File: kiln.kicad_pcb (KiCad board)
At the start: 2 copper layers, 68 parts, among them IC1 PS2702-1-F3-A, J1 SJ2-35813B-SMT-TR, J2 SJ2-35813B-SMT-TR, J3 1935174, J4 1935161, J5 1935161, K1 EE2-12SNUH, Q1 BC817-16, Q2 BC817-16, SW1 SW_Push, U1 LM7805_TO220, U2 TXS0108EPW, U3 LM1117T-3.3, U4 ADS1118IDGS, U5 MAX31856, U6 MAX31856

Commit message: more sch updates
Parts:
- removed A1: Arduino_Nano_v3.x, Module:Arduino_Nano
- removed A2: Arduino_Nano_ESP32, Module:Arduino_Nano
- removed C1, C5: 10uf, Capacitor_SMD:C_0402_1005Metric
- removed C10, C4: 10uf 16v, Capacitor_SMD:C_0402_1005Metric
- removed C11: 0.001uf, Capacitor_SMD:C_0402_1005Metric
- removed C12, C14, C17, C19: 0.01uf, Capacitor_SMD:C_0402_1005Metric
- removed C13, C15, C16, C18, C2, C20, C21, C3, C6, C9: 0.1uf, Capacitor_SMD:C_0402_1005Metric
- removed C7, C8: 10u, Capacitor_SMD:C_0805_2012Metric
- removed D1, D2, D3, D4, D5, D6, D7, D8, D9: SS16FP, SamacSys_Parts:SS12FP
- removed IC1: PS2702-1-F3-A, SamacSys_Parts:SOP254P700X230-4N
- removed J1, J2: SJ2-35813B-SMT-TR, SamacSys_Parts:SJ235813BSMTTR
- removed J3: 1935174, SamacSys_Parts:1935174
- removed J4, J5: 1935161, SamacSys_Parts:1935161
- removed K1: EE2-12SNUH, Relay_SMD:Relay_DPDT_Kemet_EE2_NUH
- removed Q1, Q2: BC817-16, Package_TO_SOT_SMD:SOT-23
- removed R1, R5, R6, R9: 1k, Resistor_SMD:R_0402_1005Metric
- removed R10, R13, R14, R15, R18, R19, R20: 10k, Resistor_SMD:R_0402_1005Metric
- removed R11, R12, R16, R17: 100, Resistor_SMD:R_0402_1005Metric
- removed R2: 220R 1/8W, Resistor_SMD:R_0805_2012Metric
- removed R3, R4: 100R 1W, Resistor_SMD:R_2512_6332Metric
- removed R7, R8: 47k, Resistor_SMD:R_0402_1005Metric
- removed SW1: SW_Push, Button_Switch_SMD:SW_Push_1P1T_NO_E-Switch_TL3301NxxxxxG
- removed U1: LM7805_TO220, Package_TO_SOT_THT:TO-220-3_Vertical
- removed U2: TXS0108EPW, Package_SO:TSSOP-20_4.4x6.5mm_P0.65mm
- removed U3: LM1117T-3.3, Package_TO_SOT_THT:TO-220-3_Vertical
- removed U4: ADS1118IDGS, Package_SO:VSSOP-10_3x3mm_P0.5mm
- removed U5, U6: MAX31856, Package_SO:TSSOP-14_4.4x5mm_P0.65mm

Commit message: progress on pcb
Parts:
- added A1: Arduino_Nano_v3.x, Module:Arduino_Nano, F.Cu at (209.3, 57.8)
- added A2: Arduino_Nano_v3.x, Module:Arduino_Nano, F.Cu at (125.1, 59.0)
- added C1: 10uf 16v, Capacitor_SMD:C_0805_2012Metric, F.Cu at (178.8, 81.3)
- added C10: 0.01uf, Capacitor_SMD:C_0402_1005Metric, F.Cu at (212.5, 47.3)
- added C11: 0.01uf, Capacitor_SMD:C_0402_1005Metric, F.Cu at (121.5, 77.5)
- added C12: 470u 35v, Capacitor_SMD:CP_Elec_10x14.3, F.Cu at (27.8, 69.0)
- added C13: 2.2uF, Capacitor_SMD:C_1206_3216Metric, F.Cu at (37.5, 79.5)
- added C14: 10uf 16v, Capacitor_SMD:C_0805_2012Metric, F.Cu at (85.0, 80.2)
- added C15: 0.1uf, Capacitor_SMD:C_0402_1005Metric, F.Cu at (85.0, 82.7)
- added C16: 0.1uf, Capacitor_SMD:C_0402_1005Metric, F.Cu at (43.5, 87.5)
- added C17: 0.1uf, Capacitor_SMD:C_0402_1005Metric, F.Cu at (77.0, 82.7)
- added C18: 2.2uF, Capacitor_SMD:C_1206_3216Metric, F.Cu at (52.0, 82.5)
- added C19: 10uf 16v, Capacitor_SMD:C_0805_2012Metric, F.Cu at (77.0, 80.2)
- added C2: 0.1uf, Capacitor_SMD:C_0402_1005Metric, F.Cu at (177.8, 83.3)
- added C20: 0.1uf, Capacitor_SMD:C_0402_1005Metric, F.Cu at (51.5, 79.0)
- added C21: 4.7pF, Capacitor_SMD:C_0402_1005Metric, F.Cu at (53.5, 86.0)
- added C22: 0.1uf, Capacitor_SMD:C_0402_1005Metric, F.Cu at (72.0, 82.7)
- added C23: 47uF 16V, Capacitor_SMD:C_1210_3225Metric, F.Cu at (56.5, 87.5)
- added C24: 10uf 16v, Capacitor_SMD:C_0805_2012Metric, F.Cu at (72.0, 80.2)
- added C25: 0.01uf, Capacitor_SMD:C_0402_1005Metric, F.Cu at (170.8, 28.8)
- added C26: 0.1uf, Capacitor_SMD:C_0402_1005Metric, F.Cu at (171.8, 30.8)
- added C27: 0.01uf, Capacitor_SMD:C_0402_1005Metric, F.Cu at (172.8, 28.8)
- added C28: 0.1uf, Capacitor_SMD:C_0402_1005Metric, F.Cu at (167.9, 41.1)
- added C29: 0.1uf, Capacitor_SMD:C_0402_1005Metric, F.Cu at (169.4, 41.1)
- added C3: 0.1uf, Capacitor_SMD:C_0402_1005Metric, F.Cu at (175.4, 83.3)
- added C30: 0.01uf, Capacitor_SMD:C_0402_1005Metric, F.Cu at (98.5, 28.5)
- added C31: 0.1uf, Capacitor_SMD:C_0402_1005Metric, F.Cu at (99.5, 30.5)
- added C32: 0.01uf, Capacitor_SMD:C_0402_1005Metric, F.Cu at (100.5, 28.5)
- added C33: 0.1uf, Capacitor_SMD:C_0402_1005Metric, F.Cu at (95.5, 40.9)
- added C34: 0.1uf, Capacitor_SMD:C_0402_1005Metric, F.Cu at (97.0, 40.9)
- added C35: 0.01uf, Capacitor_SMD:C_0402_1005Metric, F.Cu at (111.0, 28.5)
- added C36: 0.1uf, Capacitor_SMD:C_0402_1005Metric, F.Cu at (112.0, 30.5)
- added C37: 0.01uf, Capacitor_SMD:C_0402_1005Metric, F.Cu at (113.0, 28.5)
- added C38: 0.1uf, Capacitor_SMD:C_0402_1005Metric, F.Cu at (108.0, 40.9)
- added C39: 0.1uf, Capacitor_SMD:C_0402_1005Metric, F.Cu at (109.5, 40.9)
- added C4: 10uf 16v, Capacitor_SMD:C_0805_2012Metric, F.Cu at (174.8, 81.3)
- added C40: 0.01uf, Capacitor_SMD:C_0402_1005Metric, F.Cu at (123.5, 28.5)
- added C41: 0.1uf, Capacitor_SMD:C_0402_1005Metric, F.Cu at (124.5, 30.5)
- added C42: 0.01uf, Capacitor_SMD:C_0402_1005Metric, F.Cu at (125.5, 28.5)
- added C43: 0.1uf, Capacitor_SMD:C_0402_1005Metric, F.Cu at (122.0, 40.9)
- added C44: 0.1uf, Capacitor_SMD:C_0402_1005Metric, F.Cu at (120.5, 40.9)
- added C45: 0.01uf, Capacitor_SMD:C_0402_1005Metric, F.Cu at (136.0, 28.5)
- added C46: 0.1uf, Capacitor_SMD:C_0402_1005Metric, F.Cu at (137.0, 30.5)
- added C47: 0.01uf, Capacitor_SMD:C_0402_1005Metric, F.Cu at (138.0, 28.5)
- added C48: 0.1uf, Capacitor_SMD:C_0402_1005Metric, F.Cu at (134.6, 40.9)
- added C49: 0.1uf, Capacitor_SMD:C_0402_1005Metric, F.Cu at (133.1, 40.9)
- added C5: 0.1uf, Capacitor_SMD:C_0402_1005Metric, F.Cu at (167.3, 83.3)
- added C50: 10uf 16v, Capacitor_SMD:C_0805_2012Metric, F.Cu at (206.5, 42.5)
- added C6: 10uf 16v, Capacitor_SMD:C_0805_2012Metric, F.Cu at (183.8, 34.5)
- added C7: 10uf 16v, Capacitor_SMD:C_0805_2012Metric, F.Cu at (208.0, 34.6)
- added C8: 10uf 16v, Capacitor_SMD:C_0805_2012Metric, F.Cu at (166.8, 81.3)
- added C9: 0.01uf, Capacitor_SMD:C_0402_1005Metric, F.Cu at (212.0, 89.0)
- added D1: SS16FP, SamacSys_Parts:SS12FP, F.Cu at (181.9, 29.0)
- added D10: SS16FP, SamacSys_Parts:SS12FP, F.Cu at (103.0, 45.5)
- added D11: SS16FP, SamacSys_Parts:SS12FP, F.Cu at (116.0, 45.5)
- added D12: SS16FP, SamacSys_Parts:SS12FP, F.Cu at (127.5, 45.5)
- added D13: SS16FP, SamacSys_Parts:SS12FP, F.Cu at (140.0, 45.6)
- added D14: SS16FP, SamacSys_Parts:SS12FP, F.Cu at (96.0, 36.4)
- added D15: SS16FP, SamacSys_Parts:SS12FP, F.Cu at (108.5, 36.5)
- added D16: SS16FP, SamacSys_Parts:SS12FP, F.Cu at (121.0, 36.4)
- added D17: SS16FP, SamacSys_Parts:SS12FP, F.Cu at (133.5, 36.5)
- added D18: SS16FP, SamacSys_Parts:SS12FP, F.Cu at (50.0, 34.6)
- added D19: SMAJ24CA, Diode_SMD:D_SMA, F.Cu at (53.4, 44.7)
- added D2: SS16FP, SamacSys_Parts:SS12FP, F.Cu at (187.4, 29.0)
- added D20: SS16FP, SamacSys_Parts:SS12FP, F.Cu at (29.9, 34.4)
- added D21: SMAJ24CA, Diode_SMD:D_SMA, F.Cu at (33.3, 44.5)
- added D22: SMAJ24CA, Diode_SMD:D_SMA, F.Cu at (27.8, 78.0)
- added D23: SS16FP, SamacSys_Parts:SS12FP, F.Cu at (70.0, 34.6)
- added D24: SMAJ24CA, Diode_SMD:D_SMA, F.Cu at (73.3, 44.7)
- added D25: SS16FP, SamacSys_Parts:SS12FP, F.Cu at (146.3, 34.9)
- added D26: SMAJ24CA, Diode_SMD:D_SMA, F.Cu at (149.7, 45.0)
- added D3: SS16FP, SamacSys_Parts:SS12FP, F.Cu at (206.0, 29.1)
- added D4: SS16FP, SamacSys_Parts:SS12FP, F.Cu at (211.6, 29.1)
- added D5: SS16FP, SamacSys_Parts:SS12FP, F.Cu at (181.4, 32.0)
- added D6: SS16FP, SamacSys_Parts:SS12FP, F.Cu at (187.8, 32.0)
- added D7: SS16FP, SamacSys_Parts:SS12FP, F.Cu at (205.6, 32.1)
- added D8: SS16FP, SamacSys_Parts:SS12FP, F.Cu at (211.9, 32.1)
- added D9: SMAJ24CA, Diode_SMD:D_SMA, F.Cu at (215.5, 47.3)
- added FB1: 74269244182, Inductor_SMD:L_0402_1005Metric_Pad0.77x0.64mm_HandSolder, F.Cu at (168.8, 28.8)
- added FB10: 74269244182, Inductor_SMD:L_0402_1005Metric_Pad0.77x0.64mm_HandSolder, F.Cu at (140.0, 28.5)
- added FB2: 74269244182, Inductor_SMD:L_0402_1005Metric_Pad0.77x0.64mm_HandSolder, F.Cu at (174.8, 28.8)
- added FB3: 74269244182, Inductor_SMD:L_0402_1005Metric_Pad0.77x0.64mm_HandSolder, F.Cu at (96.5, 28.5)
- added FB4: 74269244182, Inductor_SMD:L_0402_1005Metric_Pad0.77x0.64mm_HandSolder, F.Cu at (102.5, 28.5)
- added FB5: 74269244182, Inductor_SMD:L_0402_1005Metric_Pad0.77x0.64mm_HandSolder, F.Cu at (109.0, 28.5)
- added FB6: 74269244182, Inductor_SMD:L_0402_1005Metric_Pad0.77x0.64mm_HandSolder, F.Cu at (115.0, 28.5)
- added FB7: 74269244182, Inductor_SMD:L_0402_1005Metric_Pad0.77x0.64mm_HandSolder, F.Cu at (121.5, 28.5)
- added FB8: 74269244182, Inductor_SMD:L_0402_1005Metric_Pad0.77x0.64mm_HandSolder, F.Cu at (127.5, 28.5)
- added FB9: 74269244182, Inductor_SMD:L_0402_1005Metric_Pad0.77x0.64mm_HandSolder, F.Cu at (134.0, 28.5)
- added IC1: LT8631IFE#PBF, SamacSys_Parts:SOP65P640X120-21N, F.Cu at (45.6, 82.9)
- added J1: 1935161, SamacSys_Parts:1935161, F.Cu at (186.8, 22.5)
- added J10: 1935161, SamacSys_Parts:1935161, F.Cu at (25.3, 86.0)
- added J11: 1935161, SamacSys_Parts:1935161, F.Cu at (174.3, 22.3)
- added J12: 1935161, SamacSys_Parts:1935161, F.Cu at (102.0, 22.0)
- added J13: 1935161, SamacSys_Parts:1935161, F.Cu at (114.5, 22.0)
- added J14: 1935174, SamacSys_Parts:1935174, F.Cu at (84.5, 22.0)
- added J15: 1935161, SamacSys_Parts:1935161, F.Cu at (127.0, 22.0)
- added J16: 1935174, SamacSys_Parts:1935174, F.Cu at (160.8, 22.3)
- added J17: 1935161, SamacSys_Parts:1935161, F.Cu at (139.5, 22.0)
- added J2: 1935161, SamacSys_Parts:1935161, F.Cu at (211.0, 22.6)
- added J3: SJ2-35813B-SMT-TR, SamacSys_Parts:SJ235813BSMTTR, F.Cu at (196.3, 24.5)
- added J4: SJ2-35813B-SMT-TR, SamacSys_Parts:SJ235813BSMTTR, F.Cu at (220.5, 24.6)
- added J5: 1935161, SamacSys_Parts:1935161, F.Cu at (223.0, 49.8)
- added J6: 1935161, SamacSys_Parts:1935161, F.Cu at (148.5, 86.0)
- added J7: 1935161, SamacSys_Parts:1935161, F.Cu at (136.0, 86.0)
- added J8: 1935174, SamacSys_Parts:1935174, F.Cu at (64.5, 22.0)
- added J9: 1935174, SamacSys_Parts:1935174, F.Cu at (44.4, 21.8)
- added K1: EE2-12SNUH, Relay_SMD:Relay_DPDT_Kemet_EE2_NUH, F.Cu at (59.9, 35.1)
- added K2: EE2-12SNUH, Relay_SMD:Relay_DPDT_Kemet_EE2_NUH, F.Cu at (39.7, 34.9)
- added K3: EE2-12SNUH, Relay_SMD:Relay_DPDT_Kemet_EE2_NUH, F.Cu at (79.8, 35.1)
- added K4: EE2-12SNUH, Relay_SMD:Relay_DPDT_Kemet_EE2_NUH, F.Cu at (156.0, 35.4)
- added L1: 15u (14.2u) 2A, Inductor_SMD:L_Chilisin_BMRF00101040, F.Cu at (59.0, 78.0)
- added Q1: BSP296NH6327XTSA1, Package_TO_SOT_SMD:SOT-223-3_TabPin2, F.Cu at (61.0, 44.5)
- added Q2: BSP296NH6327XTSA1, Package_TO_SOT_SMD:SOT-223-3_TabPin2, F.Cu at (40.9, 44.3)
- added Q3: BSP296NH6327XTSA1, Package_TO_SOT_SMD:SOT-223-3_TabPin2, F.Cu at (81.0, 44.5)
- added Q4: BSP296NH6327XTSA1, Package_TO_SOT_SMD:SOT-223-3_TabPin2, F.Cu at (157.3, 44.8)
- added R1: 100R 1W, Resistor_SMD:R_2512_6332Metric, F.Cu at (194.3, 35.5)
- added R10: 10k, Resistor_SMD:R_0402_1005Metric, F.Cu at (173.3, 76.4)
- added R11: 10k, Resistor_SMD:R_0402_1005Metric, F.Cu at (173.3, 54.4)
- added R12: 680, Resistor_SMD:R_0402_1005Metric, F.Cu at (200.5, 77.5)
- added R13: 10k, Resistor_SMD:R_0402_1005Metric, F.Cu at (209.5, 89.0)
- added R14: 1k, Resistor_SMD:R_0402_1005Metric, F.Cu at (191.8, 77.7)
- added R15: 1k, Resistor_SMD:R_0402_1005Metric, F.Cu at (187.0, 77.6)
- added R16: 1k, Resistor_SMD:R_0402_1005Metric, F.Cu at (212.5, 44.8)
- added R17: 680, Resistor_SMD:R_0402_1005Metric, F.Cu at (191.8, 85.2)
- added R18: 680, Resistor_SMD:R_0402_1005Metric, F.Cu at (187.0, 85.1)
- added R19: 10k, Resistor_SMD:R_0402_1005Metric, F.Cu at (125.0, 46.5)
- added R2: 100R 1W, Resistor_SMD:R_2512_6332Metric, F.Cu at (218.5, 35.6)
- added R20: 10k, Resistor_SMD:R_0402_1005Metric, F.Cu at (102.5, 56.0)
- added R21: 10k, Resistor_SMD:R_0402_1005Metric, F.Cu at (118.5, 38.5)
- added R22: 10k, Resistor_SMD:R_0402_1005Metric, F.Cu at (100.0, 56.0)
- added R23: 10k, Resistor_SMD:R_0402_1005Metric, F.Cu at (97.0, 56.0)
- added R24: 10k, Resistor_SMD:R_0402_1005Metric, F.Cu at (95.0, 56.0)
- added R25: 10k, Resistor_SMD:R_0402_1005Metric, F.Cu at (92.5, 56.0)
- added R26: 0, Resistor_SMD:R_0805_2012Metric, F.Cu at (115.5, 49.5)
- added R27: 10k, Resistor_SMD:R_0402_1005Metric, F.Cu at (89.0, 56.0)
- added R28: 10k, Resistor_SMD:R_0402_1005Metric, F.Cu at (88.5, 77.0)
- added R29: 0, Resistor_SMD:R_0805_2012Metric, F.Cu at (115.5, 52.5)
- added R3: 1k, Resistor_SMD:R_0402_1005Metric, F.Cu at (186.8, 34.5)
- added R30: 0, Resistor_SMD:R_0805_2012Metric, F.Cu at (140.5, 69.9)
- added R31: 0, Resistor_SMD:R_0805_2012Metric, F.Cu at (92.0, 78.0)
- added R32: 0, Resistor_SMD:R_0805_2012Metric, F.Cu at (140.5, 74.4)
- added R33: 10k, Resistor_SMD:R_0402_1005Metric, F.Cu at (119.0, 77.5)
- added R34: 1k, Resistor_SMD:R_0402_1005Metric, F.Cu at (110.5, 77.0)
- added R35: 120, Resistor_SMD:R_0402_1005Metric, F.Cu at (145.0, 80.0)
- added R36: 120, Resistor_SMD:R_0402_1005Metric, F.Cu at (66.8, 44.7)
- added R37: 10k, Resistor_SMD:R_0402_1005Metric, F.Cu at (64.3, 49.2)
- added R38: 0, Resistor_SMD:R_1206_3216Metric, B.Cu at (56.5, 28.5)
- added R39: 0, Resistor_SMD:R_1206_3216Metric, B.Cu at (36.4, 28.3)
- added R4: 1k, Resistor_SMD:R_0402_1005Metric, F.Cu at (211.0, 34.6)
- added R40: 120, Resistor_SMD:R_0402_1005Metric, F.Cu at (46.8, 44.5)
- added R41: 10k, Resistor_SMD:R_0402_1005Metric, F.Cu at (44.3, 49.0)
- added R42: 0, Resistor_SMD:R_1206_3216Metric, B.Cu at (76.5, 28.5)
- added R43: 0, Resistor_SMD:R_1206_3216Metric, B.Cu at (152.9, 28.8)
- added R44: 75k, Resistor_SMD:R_0402_1005Metric, F.Cu at (40.5, 79.0)
- added R45: 10k, Resistor_SMD:R_0402_1005Metric, F.Cu at (40.0, 81.0)
- added R46: 8.66k, Resistor_SMD:R_0402_1005Metric, F.Cu at (39.5, 84.5)
- added R47: 422k, Resistor_SMD:R_0402_1005Metric, F.Cu at (52.0, 86.0)
- added R48: 47.5k, Resistor_SMD:R_0402_1005Metric, F.Cu at (52.0, 88.5)
- added R49: 120, Resistor_SMD:R_0402_1005Metric, F.Cu at (169.3, 30.8)
- added R5: 47.5k, Resistor_SMD:R_0402_1005Metric, F.Cu at (183.8, 36.5)
- added R50: 120, Resistor_SMD:R_0402_1005Metric, F.Cu at (174.3, 30.8)
- added R51: 10k, Resistor_SMD:R_0402_1005Metric, F.Cu at (171.4, 42.6)
- added R52: 10k, Resistor_SMD:R_0402_1005Metric, B.Cu at (171.4, 43.6)
- added R53: 10k, Resistor_SMD:R_0402_1005Metric, F.Cu at (171.4, 44.6)
- added R54: 120, Resistor_SMD:R_0402_1005Metric, F.Cu at (97.0, 30.5)
- added R55: 120, Resistor_SMD:R_0402_1005Metric, F.Cu at (102.0, 30.5)
- added R56: 10k, Resistor_SMD:R_0402_1005Metric, F.Cu at (99.0, 42.4)
- added R57: 10k, Resistor_SMD:R_0402_1005Metric, B.Cu at (99.0, 43.4)
- added R58: 10k, Resistor_SMD:R_0402_1005Metric, F.Cu at (99.0, 44.4)
- added R59: 120, Resistor_SMD:R_0402_1005Metric, F.Cu at (109.5, 30.5)
- added R6: 47.5k, Resistor_SMD:R_0402_1005Metric, F.Cu at (208.0, 36.6)
- added R60: 120, Resistor_SMD:R_0402_1005Metric, F.Cu at (114.5, 30.5)
- added R61: 10k, Resistor_SMD:R_0402_1005Metric, F.Cu at (111.5, 42.4)
- added R62: 10k, Resistor_SMD:R_0402_1005Metric, B.Cu at (111.5, 43.4)
- added R63: 10k, Resistor_SMD:R_0402_1005Metric, F.Cu at (111.5, 44.4)
- added R64: 120, Resistor_SMD:R_0402_1005Metric, F.Cu at (86.8, 44.7)
- added R65: 10k, Resistor_SMD:R_0402_1005Metric, F.Cu at (84.3, 49.2)
- added R68: 120, Resistor_SMD:R_0402_1005Metric, F.Cu at (122.0, 30.5)
- added R69: 120, Resistor_SMD:R_0402_1005Metric, F.Cu at (127.0, 30.5)
- added R7: 10k, Resistor_SMD:R_0402_1005Metric, F.Cu at (181.3, 54.4)
- added R70: 10k, Resistor_SMD:R_0402_1005Metric, F.Cu at (124.0, 42.4)
- added R71: 10k, Resistor_SMD:R_0402_1005Metric, B.Cu at (124.0, 43.4)
- added R72: 10k, Resistor_SMD:R_0402_1005Metric, F.Cu at (124.0, 44.4)
- added R73: 120, Resistor_SMD:R_0402_1005Metric, F.Cu at (163.2, 45.0)
- added R74: 10k, Resistor_SMD:R_0402_1005Metric, F.Cu at (160.7, 49.5)
- added R77: 120, Resistor_SMD:R_0402_1005Metric, F.Cu at (134.5, 30.5)
- added R78: 120, Resistor_SMD:R_0402_1005Metric, F.Cu at (139.5, 30.5)
- added R79: 10k, Resistor_SMD:R_0402_1005Metric, F.Cu at (136.6, 42.4)
- added R8: 10k, Resistor_SMD:R_0402_1005Metric, F.Cu at (178.8, 54.4)
- added R80: 10k, Resistor_SMD:R_0402_1005Metric, B.Cu at (136.6, 43.4)
- added R81: 10k, Resistor_SMD:R_0402_1005Metric, F.Cu at (136.6, 44.4)
- added R82: 0, Resistor_SMD:R_1206_3216Metric, F.Cu at (65.0, 28.5)
- added R83: 0, Resistor_SMD:R_1206_3216Metric, F.Cu at (44.9, 28.3)
- added R84: 0, Resistor_SMD:R_1206_3216Metric, F.Cu at (85.0, 28.5)
- added R85: 0, Resistor_SMD:R_1206_3216Metric, F.Cu at (161.3, 28.8)
- added R9: 10k, Resistor_SMD:R_0402_1005Metric, F.Cu at (176.3, 54.4)
- added SW1: SW_Push, Button_Switch_SMD:SW_Push_1P1T_NO_E-Switch_TL3301NxxxxxG, F.Cu at (210.3, 81.8)
- added SW2: SW_Push, Button_Switch_SMD:SW_Push_1P1T_NO_E-Switch_TL3301NxxxxxG, F.Cu at (121.0, 84.5)
- added U1: LM7805_TO220, Package_TO_SOT_THT:TO-220-3_Vertical, F.Cu at (179.4, 86.3)
- added U10: MAX3490xSA, Package_SO:SOIC-8_3.9x4.9mm_P1.27mm, F.Cu at (135.0, 76.5)
- added U11: LM7805_TO220, Package_TO_SOT_THT:TO-220-3_Vertical, F.Cu at (86.1, 86.3)
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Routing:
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- added copper zone on B.Cu, net GND
- added copper zone on F.Cu, net GND
- added copper zone on B.Cu, net GND_Safty
- added copper zone on F.Cu, net GND_Safty
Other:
- board outline added: 211 x 74 mm

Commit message: progress
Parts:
- removed A2: Arduino_Nano_v3.x, Module:Arduino_Nano
- removed FB10, FB9: 74269244182, Inductor_SMD:L_0402_1005Metric_Pad0.77x0.64mm_HandSolder
- removed SW1, SW2: SW_Push, Button_Switch_SMD:SW_Push_1P1T_NO_E-Switch_TL3301NxxxxxG
- removed U13, U14, U15, U16, U17: MAX31856, Package_SO:TSSOP-14_4.4x5mm_P0.65mm
- added C51: 0.1uf, Capacitor_SMD:C_0402_1005Metric, F.Cu at (92.0, 95.8)
- added C52: 10uf 16v, Capacitor_SMD:C_0805_2012Metric, F.Cu at (89.0, 86.0)
- added C53: 470uf 50v, SamacSys_Parts:CAPAE1360X1450N, F.Cu at (88.1, 38.7)
- added C54: 2.2uF, Capacitor_SMD:C_1206_3216Metric, F.Cu at (99.7, 40.6)
- added C55: 0.1uf, Capacitor_SMD:C_0402_1005Metric, F.Cu at (107.1, 31.7)
- added C56: 2.2uF, Capacitor_SMD:C_1206_3216Metric, F.Cu at (99.7, 43.9)
- added C57: 0.1uf, Capacitor_SMD:C_0402_1005Metric, F.Cu at (107.1, 33.7)
- added C58: 4.7pF, Capacitor_SMD:C_0402_1005Metric, F.Cu at (107.1, 35.7)
- added C59: 47uF 16V, Capacitor_SMD:C_1210_3225Metric, F.Cu at (106.3, 57.6)
- added C60: 0.1uf, Capacitor_SMD:C_0402_1005Metric, F.Cu at (107.1, 37.6)
- added C61: 470uf 50v, SamacSys_Parts:CAPAE1360X1450N, F.Cu at (88.1, 7.42)
- added C62: 2.2uF, Capacitor_SMD:C_1206_3216Metric, F.Cu at (99.7, 9.35)
- added C63: 0.1uf, Capacitor_SMD:C_0402_1005Metric, F.Cu at (107.1, 0.48)
- added C64: 2.2uF, Capacitor_SMD:C_1206_3216Metric, F.Cu at (99.7, 12.7)
- added C65: 0.1uf, Capacitor_SMD:C_0402_1005Metric, F.Cu at (107.1, 2.46)
- added C66: 4.7pF, Capacitor_SMD:C_0402_1005Metric, F.Cu at (107.1, 4.42)
- added C67: 47uF 16V, Capacitor_SMD:C_1210_3225Metric, F.Cu at (106.3, 26.3)
- added C68: 0.1uf, Capacitor_SMD:C_0402_1005Metric, F.Cu at (107.1, 6.39)
- added D27: LED, LED_SMD:LED_0402_1005Metric, F.Cu at (106.5, 16.3)
- added IC2: LT8631IFE#PBF, SamacSys_Parts:SOP65P640X120-21N, F.Cu at (101.3, 34.9)
- added IC3: LT8631IFE#PBF, SamacSys_Parts:SOP65P640X120-21N, F.Cu at (101.3, 3.60)
- added J18: 1935161, SamacSys_Parts:1935161, F.Cu at (83.4, 52.1)
- added J19: 1935161, SamacSys_Parts:1935161, F.Cu at (83.4, 20.9)
- added K5: EE2-12NUH, Relay_SMD:Relay_DPDT_Kemet_EE2_NUH, F.Cu at (116.0, 19.9)
- added L2: 4.7uH 3.16A, Inductor_SMD:L_7.3x7.3_H4.5, F.Cu at (100.1, 51.0)
- added L3: 4.7uH 3.16A, Inductor_SMD:L_7.3x7.3_H4.5, F.Cu at (100.1, 19.8)
- added Q5: BSS138P,215, Package_TO_SOT_SMD:SOT-23, F.Cu at (129.0, 13.8)
- added R100: 10k, Resistor_SMD:R_0402_1005Metric, F.Cu at (93.9, 18.3)
- added R101: 8.66k, Resistor_SMD:R_0402_1005Metric, F.Cu at (93.9, 20.3)
- added R102: 475k 1%, Resistor_SMD:R_0402_1005Metric, F.Cu at (93.9, 22.3)
- added R103: 154k 1%, Resistor_SMD:R_0402_1005Metric, F.Cu at (93.9, 24.3)
- added R66: 0, Resistor_SMD:R_1206_3216Metric, B.Cu at (-36.0, 103.5)
- added R67: 0, Resistor_SMD:R_1206_3216Metric, B.Cu at (-42.0, 103.5)
- added R75: 47k, Resistor_SMD:R_0402_1005Metric, F.Cu at (54.7, 123.9)
- added R76: 47k, Resistor_SMD:R_0402_1005Metric, F.Cu at (54.7, 125.9)
- added R86: 47k, Resistor_SMD:R_0402_1005Metric, F.Cu at (84.2, 92.3)
- added R87: 47k, Resistor_SMD:R_0402_1005Metric, F.Cu at (84.2, 94.3)
- added R88: 47k, Resistor_SMD:R_0402_1005Metric, F.Cu at (84.2, 96.3)
- added R89: 1M, Resistor_SMD:R_0402_1005Metric, F.Cu at (84.2, 98.3)
- added R90: 2.2k, Resistor_SMD:R_0805_2012Metric, F.Cu at (104.7, 40.4)
- added R91: 2.2k, Resistor_SMD:R_0805_2012Metric, F.Cu at (104.7, 43.3)
- added R92: 75k, Resistor_SMD:R_0402_1005Metric, F.Cu at (93.9, 47.6)
- added R93: 10k, Resistor_SMD:R_0402_1005Metric, F.Cu at (93.9, 49.6)
- added R94: 8.66k, Resistor_SMD:R_0402_1005Metric, F.Cu at (93.9, 51.6)
- added R95: 475k 1%, Resistor_SMD:R_0402_1005Metric, F.Cu at (93.9, 53.6)
- added R96: 154k 1%, Resistor_SMD:R_0402_1005Metric, F.Cu at (93.9, 55.6)
- added R97: 2.2k, Resistor_SMD:R_0805_2012Metric, F.Cu at (104.7, 9.14)
- added R98: 2.2k, Resistor_SMD:R_0805_2012Metric, F.Cu at (104.7, 12.1)
- added R99: 75k, Resistor_SMD:R_0402_1005Metric, F.Cu at (93.9, 16.3)
- A1: value Arduino_Nano_v3.x -> RaspberryPi_Pico; footprint Module:Arduino_Nano -> Module:RaspberryPi_Pico_Common_Unspecified
- C1, C24, C4, C6: value 10uf 16v -> 0.1uf; footprint Capacitor_SMD:C_0805_2012Metric -> Capacitor_SMD:C_0402_1005Metric
- C10: value 0.01uf -> 2.2uF; footprint Capacitor_SMD:C_0402_1005Metric -> Capacitor_SMD:C_1206_3216Metric
- C11, C27, C30, C37, C40, C45: value 0.01uf -> 0.1uf
- C12: value 470u 35v -> 2.2uF; footprint Capacitor_SMD:CP_Elec_10x14.3 -> Capacitor_SMD:C_1206_3216Metric
- C13, C18: value 2.2uF -> 0.1uf; footprint Capacitor_SMD:C_1206_3216Metric -> Capacitor_SMD:C_0402_1005Metric
- C14, C50, C7, C8: value 10uf 16v -> 4.7pF; footprint Capacitor_SMD:C_0805_2012Metric -> Capacitor_SMD:C_0402_1005Metric
- C15: value 0.1uf -> 47uF 16V; footprint Capacitor_SMD:C_0402_1005Metric -> Capacitor_SMD:C_1210_3225Metric
- C17, C20, C26, C29, C3, C31, C36, C38, C39: value 0.1uf -> 0.01uf
- C19: value 10uf 16v -> 0.01uf; footprint Capacitor_SMD:C_0805_2012Metric -> Capacitor_SMD:C_0402_1005Metric
- C2: value 0.1uf -> 2.2uF; footprint Capacitor_SMD:C_0402_1005Metric -> Capacitor_SMD:C_1206_3216Metric
- C21: value 4.7pF -> 0.1uf
- C23: value 47uF 16V -> 0.01uf; footprint Capacitor_SMD:C_1210_3225Metric -> Capacitor_SMD:C_0402_1005Metric
- C35, C42, C47: value 0.01uf -> 4.7pF
- C43, C44: value 0.1uf -> 4.7pF
- C46, C49: value 0.1uf -> 10uf 16v; footprint Capacitor_SMD:C_0402_1005Metric -> Capacitor_SMD:C_0805_2012Metric
- C9: value 0.01uf -> 470uf 50v; footprint Capacitor_SMD:C_0402_1005Metric -> SamacSys_Parts:CAPAE1360X1450N
- D11, D2, D4, D7: value SS16FP -> SMAJ24CA; footprint SamacSys_Parts:SS12FP -> Diode_SMD:D_SMA
- D12, D13, D16, D17, D20: value SS16FP -> BZX84C3V3LT1G; footprint SamacSys_Parts:SS12FP -> Package_TO_SOT_SMD:SOT-23
- D19, D22: value SMAJ24CA -> SS16FP; footprint Diode_SMD:D_SMA -> SamacSys_Parts:SS12FP
- D21: value SMAJ24CA -> BZX84C3V3LT1G; footprint Diode_SMD:D_SMA -> Package_TO_SOT_SMD:SOT-23
- D25, D5: value SS16FP -> LED; footprint SamacSys_Parts:SS12FP -> LED_SMD:LED_0402_1005Metric
- J10, J11: value 1935161 -> 1935174; footprint SamacSys_Parts:1935161 -> SamacSys_Parts:1935174
- J13, J15, J17: value 1935161 -> SJ2-35813B-SMT-TR; footprint SamacSys_Parts:1935161 -> SamacSys_Parts:SJ235813BSMTTR
- J14, J16, J9: value 1935174 -> 1935161; footprint SamacSys_Parts:1935174 -> SamacSys_Parts:1935161
- J2: value 1935161 -> Conn_01x10_Pin; footprint SamacSys_Parts:1935161 -> Connector_JST:JST_XH_B10B-XH-AM_1x10_P2.50mm_Vertical
- J3, J4: value SJ2-35813B-SMT-TR -> 1935174; footprint SamacSys_Parts:SJ235813BSMTTR -> SamacSys_Parts:1935174
- K1, K2, K3, K4: value EE2-12SNUH -> EE2-12NUH
- L1: value 15u (14.2u) 2A -> 22uH Shld 20% 1.9A MSD1048-223MED; footprint Inductor_SMD:L_Chilisin_BMRF00101040 -> Inductor_SMD:L_Bourns_SRP1038C_10.0x10.0mm
- Q1, Q2, Q3, Q4: value BSP296NH6327XTSA1 -> BSS138P,215; footprint Package_TO_SOT_SMD:SOT-223-3_TabPin2 -> Package_TO_SOT_SMD:SOT-23
- R1, R2: value 100R 1W -> 10k; footprint Resistor_SMD:R_2512_6332Metric -> Resistor_SMD:R_0402_1005Metric
- R10, R8, R9: value 10k -> 1k
- R11, R7: value 10k -> 390
- R12: value 680 -> 390
- R14, R3, R34, R4: value 1k -> 10k
- R16: value 1k -> 2.2k
- R17: value 680 -> 2.2k
- R18: value 680 -> 10k
- R26, R29, R30, R31, R32: value 0 -> 10k; footprint Resistor_SMD:R_0805_2012Metric -> Resistor_SMD:R_0402_1005Metric
- R33, R37: value 10k -> 120
- R35, R36, R40, R59, R60: value 120 -> 0; footprint Resistor_SMD:R_0402_1005Metric -> Resistor_SMD:R_1206_3216Metric
- R38: value 0 -> 10k; footprint Resistor_SMD:R_1206_3216Metric -> Resistor_SMD:R_0402_1005Metric; moved to F.Cu
- R39: moved to F.Cu
- R41: value 10k -> 2.2k; footprint Resistor_SMD:R_0402_1005Metric -> Resistor_SMD:R_0805_2012Metric
- R42: value 0 -> 2.2k; footprint Resistor_SMD:R_1206_3216Metric -> Resistor_SMD:R_0805_2012Metric; moved to F.Cu
- R43: value 0 -> 75k; footprint Resistor_SMD:R_1206_3216Metric -> Resistor_SMD:R_0402_1005Metric; moved to F.Cu
- R44: value 75k -> 10k
- R45: value 10k -> 8.66k
- R46: value 8.66k -> 475k 1%
- R47: value 422k -> 90.7k 1%
- R48: value 47.5k -> 2k
- R49, R50, R54, R55: value 120 -> 2k
- R5, R6: value 47.5k -> 10k
- R51, R53, R56, R61, R63: value 10k -> 2k
- R52, R62: value 10k -> 2k; moved to F.Cu
- R57: value 10k -> 120; moved to F.Cu
- R69: value 120 -> 10k
- R70: value 10k -> 0; footprint Resistor_SMD:R_0402_1005Metric -> Resistor_SMD:R_1206_3216Metric
- R71: value 10k -> 0; footprint Resistor_SMD:R_0402_1005Metric -> Resistor_SMD:R_1206_3216Metric; moved to F.Cu
- R72: value 10k -> 100R 1W; footprint Resistor_SMD:R_0402_1005Metric -> Resistor_SMD:R_2512_6332Metric
- R73: value 120 -> 475k
- R74, R81: value 10k -> 47k
- R77: value 120 -> 1M
- R78: value 120 -> 100R 1W; footprint Resistor_SMD:R_0402_1005Metric -> Resistor_SMD:R_2512_6332Metric
- R79: value 10k -> 475k
- R80: value 10k -> 47k; moved to F.Cu
- R82: value 0 -> 47k; footprint Resistor_SMD:R_1206_3216Metric -> Resistor_SMD:R_0402_1005Metric
- R83: value 0 -> 1M; footprint Resistor_SMD:R_1206_3216Metric -> Resistor_SMD:R_0402_1005Metric
- R84: value 0 -> 100R 1W; footprint Resistor_SMD:R_1206_3216Metric -> Resistor_SMD:R_2512_6332Metric
- R85: value 0 -> 475k; footprint Resistor_SMD:R_1206_3216Metric -> Resistor_SMD:R_0402_1005Metric
- U1: value LM7805_TO220 -> TCMT1109; footprint Package_TO_SOT_THT:TO-220-3_Vertical -> Package_SO:SOP-4_4.4x2.6mm_P1.27mm
- U10: value MAX3490xSA -> LMV321; footprint Package_SO:SOIC-8_3.9x4.9mm_P1.27mm -> Package_TO_SOT_SMD:SOT-353_SC-70-5
- U11: value LM7805_TO220 -> LMV321; footprint Package_TO_SOT_THT:TO-220-3_Vertical -> Package_TO_SOT_SMD:SOT-353_SC-70-5
- U12: value LM1117T-3.3 -> LMV321; footprint Package_TO_SOT_THT:TO-220-3_Vertical -> Package_TO_SOT_SMD:SOT-353_SC-70-5
- U2: value LM1117T-3.3 -> TCMT1109; footprint Package_TO_SOT_THT:TO-220-3_Vertical -> Package_SO:SOP-4_4.4x2.6mm_P1.27mm
- U3: value ADS1118IDGS -> TCMT1109; footprint Package_SO:VSSOP-10_3x3mm_P0.5mm -> Package_SO:SOP-4_4.4x2.6mm_P1.27mm
- U4: value TCMT1109 -> ESP32-S3-DevKitC; footprint Package_SO:SOP-4_4.4x2.6mm_P1.27mm -> PCM_Espressif:ESP32-S3-DevKitC
- U5: value TCMT1109 -> SX1509; footprint Package_SO:SOP-4_4.4x2.6mm_P1.27mm -> PCM_SparkFun-Semiconductor-Standard:QFN-28-1EP_4x4mm_P0.4mm_EP2.6x2.6mm
- U6: value TCMT1109 -> MAX31856; footprint Package_SO:SOP-4_4.4x2.6mm_P1.27mm -> Package_SO:TSSOP-14_4.4x5mm_P0.65mm
- U7, U8, U9: value TXS0108EPW -> MAX31856; footprint Package_SO:TSSOP-20_4.4x6.5mm_P0.65mm -> Package_SO:TSSOP-14_4.4x5mm_P0.65mm
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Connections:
- A1 pad 1: unconnected-(A1-D1/TX-Pad1) -> /SaftyProcessor/MISO
- A1 pad 12: /SaftyProcessor/CS1 -> /SaftyProcessor/estop
- A1 pad 13: /SaftyProcessor/CS0 -> GND_Safty
- A1 pad 14: /SaftyProcessor/MOSI -> /SaftyProcessor/fault
- A1 pad 15: /SaftyProcessor/MISO -> unconnected-(A1-GPIO11-Pad15)
- A1 pad 16: /SaftyProcessor/CLK -> unconnected-(A1-GPIO12-Pad16)
- A1 pad 18: unconnected-(A1-AREF-Pad18) -> GND_Safty
- A1 pad 2: unconnected-(A1-D0/RX-Pad2) -> /SaftyProcessor/CS0
- A1 pad 21: Net-(A1-A2) -> unconnected-(A1-GPIO16-Pad21)
- A1 pad 22: Net-(A1-A3) -> unconnected-(A1-GPIO17-Pad22)
- A1 pad 23: Net-(A1-A4) -> GND_Safty
- A1 pad 24: Net-(A1-A5) -> unconnected-(A1-GPIO18-Pad24)
- A1 pad 27: 5v_Safty -> unconnected-(A1-GPIO21-Pad27)
- A1 pad 28: Net-(A1-~{RESET}-Pad28) -> GND_Safty
- A1 pad 29: GND_Safty -> unconnected-(A1-GPIO22-Pad29)
- A1 pad 3: unconnected-(A1-~{RESET}-Pad3) -> GND_Safty
- A1 pad 4: GND_Safty -> /SaftyProcessor/CLK
- A1 pad 5: unconnected-(A1-D2-Pad5) -> /SaftyProcessor/MOSI
- A1 pad 6: unconnected-(A1-D3-Pad6) -> /SaftyProcessor/PicoTx
- A1 pad 7: unconnected-(A1-D4-Pad7) -> /SaftyProcessor/PicoRx
- A1 pad 8: unconnected-(A1-D5-Pad8) -> GND_Safty
- C1 pad 1: 8V -> 3.3v_Safty
- C10 pad 1: Net-(A1-A2) -> 12V_Main
- C10 pad 2: GND_Safty -> GND_Main
- C11 pad 1: Net-(A2-~{RESET}-Pad28) -> Net-(IC1-TR/SS)
- C11 pad 2: GND -> GND_Main
- C12 pad 1: 12V -> Net-(IC1-INTVCC)
- C12 pad 2: GND -> GND_Main
- C13 pad 1: 12V -> Net-(IC1-SW)
- C13 pad 2: GND -> Net-(IC1-BST)
- C14 pad 1: 8V -> 5V_Main
- C14 pad 2: GND -> Net-(IC1-FB)
- C15 pad 1: 8V -> GND_Main
- C15 pad 2: GND -> 5V_Main
- C16 pad 1: Net-(IC1-TR/SS) -> 5V_Main
- C16 pad 2: GND -> GND_Main
- C17 pad 1: 5V -> GND_Safty
- C17 pad 2: GND -> Net-(U6-T+)
- C18 pad 1: Net-(IC1-INTVCC) -> Net-(U6-T+)
- C18 pad 2: GND -> Net-(U6-T-)
- C19 pad 1: 5V -> Net-(U6-T-)
- C19 pad 2: GND -> GND_Safty
- C2 pad 1: 8V -> Net-(A1-ADC_VREF)
- C20 pad 1: Net-(IC1-SW) -> Net-(U6-BIAS)
- C20 pad 2: Net-(IC1-BST) -> GND_Safty
- C21 pad 1: 8V -> 3.3v_Safty
- C21 pad 2: Net-(IC1-FB) -> GND_Safty
- C22 pad 1: 3.3V -> 3.3v_Safty
- C22 pad 2: GND -> GND_Safty
- C23 pad 1: GND -> GND_Main
- C23 pad 2: 8V -> Net-(U7-T+)
- C24 pad 1: 3.3V -> Net-(U7-T+)
- C24 pad 2: GND -> Net-(U7-T-)
- C25 pad 1: GND_Safty -> Net-(U7-T-)
- C25 pad 2: Net-(U13-T+) -> GND_Main
- C26 pad 1: Net-(U13-T+) -> Net-(U7-BIAS)
- C26 pad 2: Net-(U13-T-) -> GND_Main
- C27 pad 1: Net-(U13-T-) -> 3.3V_Main
- C27 pad 2: GND_Safty -> GND_Main
- C28 pad 1: 3.3v_Safty -> 3.3V_Main
- C28 pad 2: GND_Safty -> GND_Main
- C29 pad 1: 3.3v_Safty -> GND_Main
- C29 pad 2: GND_Safty -> Net-(U8-T+)
- C3 pad 1: 5v_Safty -> /SaftyProcessor/estop
- C30 pad 1: GND -> Net-(U8-T+)
- C30 pad 2: Net-(U14-T+) -> Net-(U8-T-)
- C31 pad 1: Net-(U14-T+) -> Net-(U8-T-)
- C31 pad 2: Net-(U14-T-) -> GND_Main
- C32 pad 1: Net-(U14-T-) -> Net-(U8-BIAS)
- C32 pad 2: GND -> GND_Main
- C33 pad 1: 3.3V -> 3.3V_Main
- C33 pad 2: GND -> GND_Main
- C34 pad 1: 3.3V -> 3.3V_Main
- C34 pad 2: GND -> GND_Main
- C35 pad 1: GND -> Net-(D7-A2)
- C35 pad 2: Net-(U15-T+) -> GND_Main
- C36 pad 1: Net-(U15-T+) -> GND_Main
- C36 pad 2: Net-(U15-T-) -> Net-(U9-T+)
- C37 pad 1: Net-(U15-T-) -> Net-(U9-T+)
- C37 pad 2: GND -> Net-(U9-T-)
- C38 pad 1: 3.3V -> Net-(U9-T-)
- C38 pad 2: GND -> GND_Main
- C39 pad 1: 3.3V -> Net-(U9-BIAS)
- C39 pad 2: GND -> GND_Main
- C4 pad 1: 5v_Safty -> 3.3V_Main
- C4 pad 2: GND_Safty -> GND_Main
- C40 pad 1: GND -> 3.3V_Main
- C40 pad 2: Net-(U16-T+) -> GND_Main
- C41 pad 1: Net-(U16-T+) -> 3.3V_Main
- C41 pad 2: Net-(U16-T-) -> GND_Main
- C42 pad 1: Net-(U16-T-) -> Net-(D9-A2)
- C42 pad 2: GND -> GND_Safty
- C43 pad 1: 3.3V -> Net-(D11-A2)
- C43 pad 2: GND -> GND_Main
- C44 pad 1: 3.3V -> Net-(D12-K)
- C44 pad 2: GND -> Net-(D13-K)
- C45 pad 1: GND -> 3.3v_Safty
- C45 pad 2: Net-(U17-T+) -> GND_Safty
- C46 pad 1: Net-(U17-T+) -> /SaftyProcessor/Current1
- C46 pad 2: Net-(U17-T-) -> GND_Safty
- C47 pad 1: Net-(U17-T-) -> Net-(D16-K)
- C47 pad 2: GND -> Net-(D17-K)
- C48 pad 1: 3.3V -> 3.3v_Safty
- C48 pad 2: GND -> GND_Safty
- C49 pad 1: 3.3V -> /SaftyProcessor/Current2
- C49 pad 2: GND -> GND_Safty
- C5 pad 1: 3.3v_Safty -> 3.3V_Main
- C5 pad 2: GND_Safty -> GND_Main
- C50 pad 1: 5v_Safty -> Net-(D20-K)
- C50 pad 2: GND_Safty -> Net-(D21-K)
- C6 pad 1: Net-(U3-AIN0) -> 5V_Main
- C6 pad 2: GND_Safty -> GND_Main
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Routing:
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- removed copper zone on B.Cu, net GND
- removed copper zone on F.Cu, net GND
- removed copper zone on B.Cu, net GND_Safty
- removed copper zone on F.Cu, net GND_Safty
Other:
- board outline removed

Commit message: progress
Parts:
- C26, C27, C28, R35, R36, R39, R40, R53, R59, R60, R70, R71: moved to B.Cu
- moved C43 212.8 mm to (-81.0, 57.0)
- moved Q5 211.7 mm to (-78.0, 58.0), turned to 180 degrees
- moved R71 208.5 mm to (-83.0, 43.5), turned to 90 degrees
- moved D11 207.2 mm to (-79.5, 54.0), turned to 180 degrees
- moved R68 206.6 mm to (-74.5, 59.0)
- moved R69 206.4 mm to (-75.0, 57.0), turned to -90 degrees
- moved D10 205.6 mm to (-79.5, 50.5), turned to 180 degrees
- moved R70 203.0 mm to (-77.0, 43.5), turned to 90 degrees
- moved C17 200.8 mm to (-65.5, 104.9)
- moved C18 200.8 mm to (-65.5, 106.9)
- moved C19 200.8 mm to (-65.5, 108.9)
- moved C20 200.8 mm to (-65.5, 110.8)
- moved C21 200.8 mm to (-65.5, 112.8)
- moved C22 200.8 mm to (-65.5, 114.8)
- moved FB1 200.8 mm to (-66.8, 117.0)
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
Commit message: small changes
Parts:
- added J20: 1935161, SamacSys_Parts:1935161, F.Cu at (-63.5, -54.3)
- added J21: 1935161, SamacSys_Parts:1935161, F.Cu at (-63.5, -42.2)
- added J23: 1935161, SamacSys_Parts:1935161, F.Cu at (-63.5, -30.1)
- added J24: 1935161, SamacSys_Parts:1935161, F.Cu at (-63.5, -18.0)
- added J25: 1935161, SamacSys_Parts:1935161, F.Cu at (-63.5, -5.86)
- moved R19 56.3 mm to (55.3, -40.4)
- moved R28 56.3 mm to (61.1, -42.4)
- moved R21 56.3 mm to (55.3, -36.4)
- moved R24 56.3 mm to (58.2, -40.4)
- moved R26 56.3 mm to (58.2, -36.4)
- moved R30 56.3 mm to (61.1, -38.4)
- moved R31 56.3 mm to (61.1, -36.4)
- moved R20 31.3 mm to (29.6, -19.0)
- moved R23 31.3 mm to (32.5, -23.0)
- moved R25 31.3 mm to (32.5, -19.0)
- moved R29 31.3 mm to (35.4, -21.0)
- moved R27 31.3 mm to (32.5, -15.0)
- moved R32 31.3 mm to (35.4, -15.0)
- moved C36 30.5 mm to (-73.7, 88.0)
- moved FB7 19.5 mm to (-73.2, 85.0)
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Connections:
- U5 pad 16: unconnected-(U5-I/O[11]-Pad16) -> /MainControler/IO_5
- U5 pad 19: unconnected-(U5-I/O[12]-Pad19) -> /MainControler/IO_6
- U5 pad 20: unconnected-(U5-I/O[13]-Pad20) -> /MainControler/IO_7
- U5 pad 5: unconnected-(U5-I/O[4]-Pad5) -> /MainControler/IO_1
- U5 pad 6: unconnected-(U5-I/O[5]-Pad6) -> /MainControler/IO_2
- U5 pad 7: unconnected-(U5-I/O[6]-Pad7) -> /MainControler/IO_3
- U5 pad 8: unconnected-(U5-I/O[7]-Pad8) -> /MainControler/IO_4

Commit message: progress
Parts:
- moved FB1 123.5 mm to (-184.3, 79.3)
- moved C17 121.4 mm to (-184.8, 82.3)
- moved FB2 121.3 mm to (-181.3, 79.3), turned to 180 degrees
- moved C20 121.0 mm to (-183.3, 83.3), turned to 180 degrees
- moved C22 120.6 mm to (-182.8, 86.8)
- moved C21 120.4 mm to (-182.8, 85.8)
- moved R48 120.1 mm to (-184.3, 80.8)
- moved C18 119.9 mm to (-182.9, 82.3)
- moved R50 119.8 mm to (-182.8, 81.3), turned to 90 degrees
- moved C19 118.3 mm to (-180.8, 82.3)
- moved R49 117.9 mm to (-181.3, 80.8), turned to 180 degrees
- moved U6 112.2 mm to (-183.3, 87.8), turned to -90 degrees
- moved J5 110.3 mm to (-180.3, 73.8)
- moved C43 100.2 mm to (-176.9, 28.1)
- moved D10 100.2 mm to (-175.4, 21.6)
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
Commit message: progress
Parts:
- C14, R46, R47: moved to B.Cu
- moved R95 152.7 mm to (236.3, 108.7)
- moved R96 152.6 mm to (236.3, 110.2)
- moved L2 151.4 mm to (243.5, 99.6)
- moved L3 150.9 mm to (250.5, 32.3)
- moved R102 150.7 mm to (243.3, 41.5)
- moved R103 150.6 mm to (243.3, 43.0)
- moved R94 150.0 mm to (232.2, 109.4)
- moved R92 149.7 mm to (232.2, 104.7)
- moved R93 149.5 mm to (232.2, 106.2)
- moved IC2 148.4 mm to (234.3, 100.6)
- moved J18 148.4 mm to (216.4, 117.9)
- moved C56 148.3 mm to (237.6, 98.5)
- moved C55 148.1 mm to (232.2, 111.0)
- moved C58 147.7 mm to (236.3, 107.2)
- moved R101 147.0 mm to (239.2, 42.2)
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
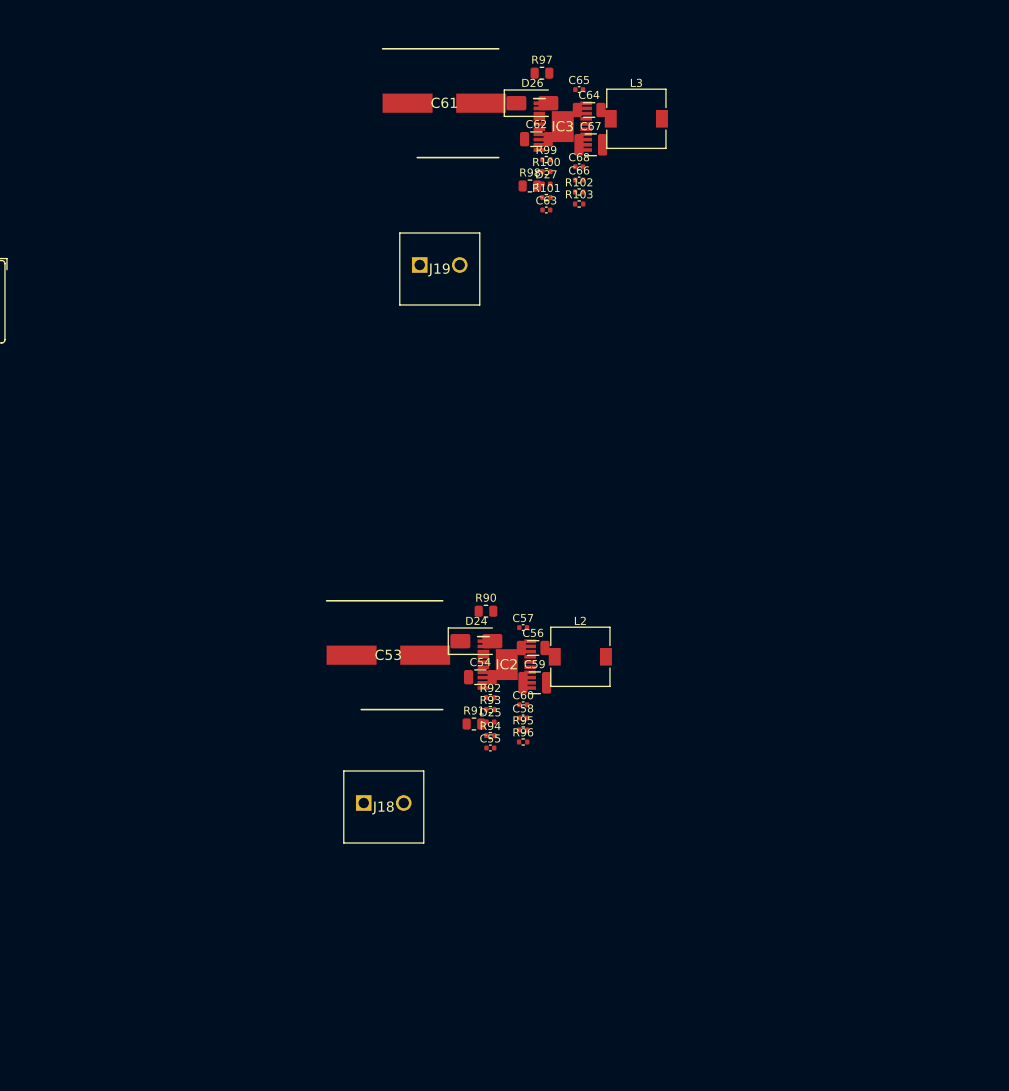
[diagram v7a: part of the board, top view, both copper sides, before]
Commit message: why does c12 have a diffrent footprint from c67 and c56
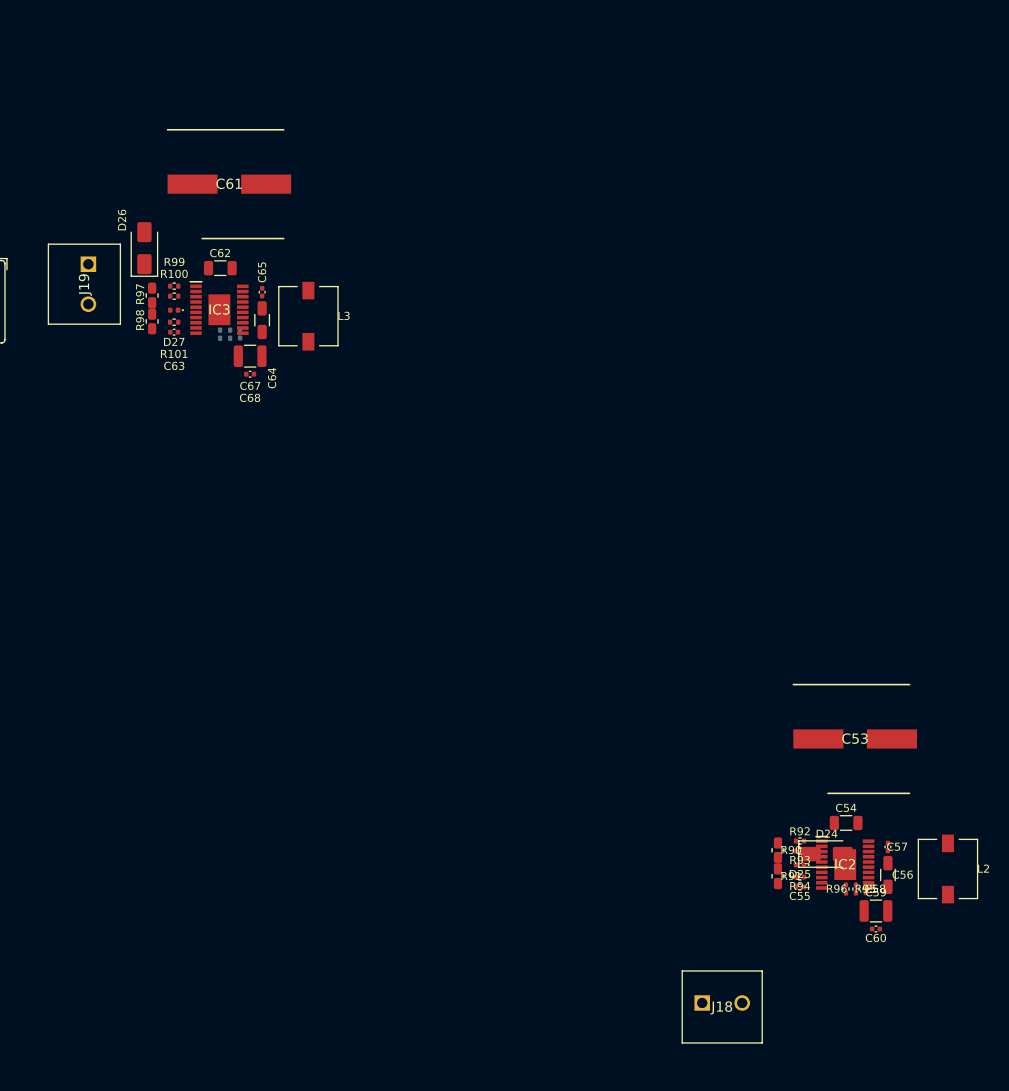
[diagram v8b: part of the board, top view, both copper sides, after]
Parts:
- C66, R102, R103: moved to B.Cu
- moved C53 59.3 mm to (277.8, 109.9)
- moved R97 56.1 mm to (190.0, 54.4), turned to -90 degrees
- moved C57 53.2 mm to (281.9, 123.4), turned to -90 degrees
- moved L2 53.1 mm to (289.4, 126.1), turned to -90 degrees
- moved C56 52.6 mm to (281.9, 126.9), turned to -90 degrees
- moved C60 52.2 mm to (280.4, 133.6), turned to 180 degrees
- moved D26 51.8 mm to (189.0, 48.5), turned to 90 degrees
- moved C59 51.3 mm to (280.4, 131.4)
- moved D24 51.3 mm to (274.3, 124.2)
- moved R98 50.2 mm to (190.0, 57.7), turned to -90 degrees
- moved C67 50.1 mm to (202.2, 62.0)
- moved C54 49.2 mm to (276.7, 120.4)
- moved IC2 49.1 mm to (276.6, 125.6)
- moved J18 49.1 mm to (258.7, 142.9)
- moved R99 49.1 mm to (192.7, 53.2)
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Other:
- board text added: "why is c12 diffrent from c64?"
